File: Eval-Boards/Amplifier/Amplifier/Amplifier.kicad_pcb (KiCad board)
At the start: 2 copper layers, 1 part

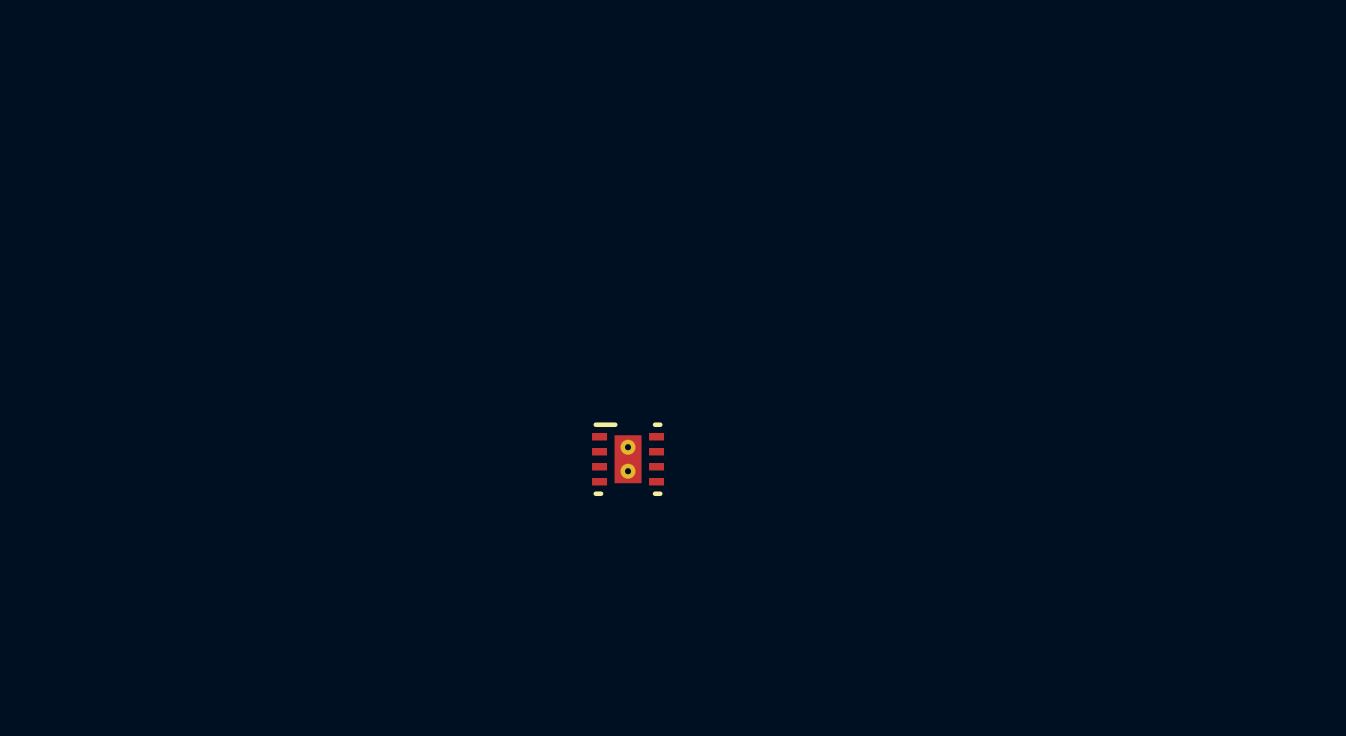
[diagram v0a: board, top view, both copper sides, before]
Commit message: New amplifier board
It looks really bad
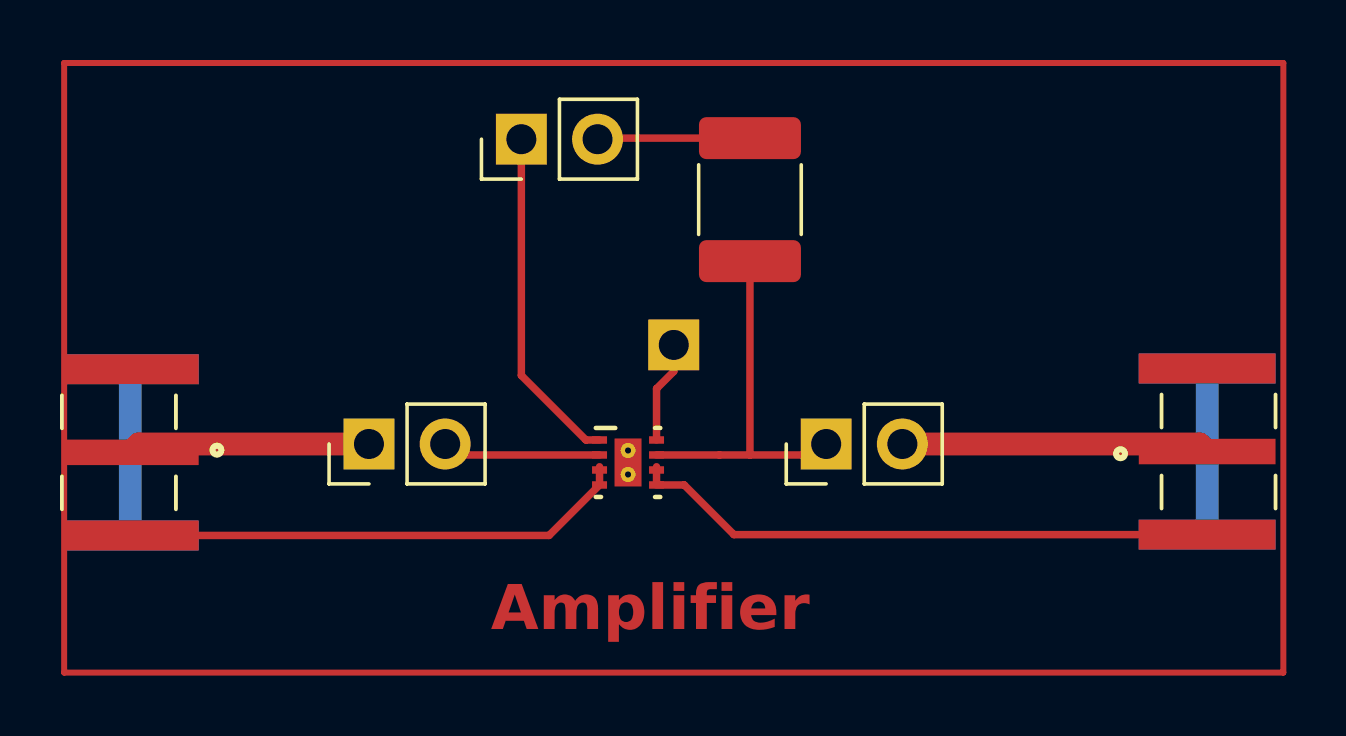
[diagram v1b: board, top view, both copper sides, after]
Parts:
- added ?: , , F.Cu at (61.0, 45.0)
- added REF**: TAOGLAS_EMPCB.SMAFSTJ.B.HT, SMA connectors:TAOGLAS_EMPCB.SMAFSTJ.B.HT, F.Cu at (42.8, 48.5)
- added REF**: PinHeader_1x02_P2.54mm_Vertical, Connector_PinHeader_2.54mm:PinHeader_1x02_P2.54mm_Vertical, F.Cu at (50.8, 48.3)
- added REF**: C_1812_4532Metric, Capacitor_SMD:C_1812_4532Metric, F.Cu at (63.5, 40.1)
- added REF**: PinHeader_1x02_P2.54mm_Vertical, Connector_PinHeader_2.54mm:PinHeader_1x02_P2.54mm_Vertical, F.Cu at (55.9, 38.1)
- added REF**: TAOGLAS_EMPCB.SMAFSTJ.B.HT, SMA connectors:TAOGLAS_EMPCB.SMAFSTJ.B.HT, F.Cu at (78.7, 48.5)
- added REF**: PinHeader_1x02_P2.54mm_Vertical, Connector_PinHeader_2.54mm:PinHeader_1x02_P2.54mm_Vertical, F.Cu at (66.0, 48.3)
- moved REF** 0.11 mm to (59.4, 48.9)
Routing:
- net (no net): track 0.00 -> 103.5 mm
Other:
- board text added: "Amplifier"

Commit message: Alot of stuff. Eval board for amp and VCO test
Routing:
- net (no net): track 103.5 -> 179.9 mm
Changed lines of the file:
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@@
   (gr_rect (start 40.64 35.56) (end 81.28 55.88)
     (stroke (width 0.2) (type default)) (fill none) (layer "F.Cu"))
-  (gr_text "Amplifier" (at 54.864 54.61) (layer "F.Cu")
+  (gr_text "Amplifier" (at 41.91 38.608) (layer "F.Cu")
     (effects (font (size 1.5 1.5) (thickness 0.3) bold) (justify left bottom))
   )
   (segment (start 63.5 48.625999) (end 65.674001 48.625999) (width 0.25) (layer "F.Cu") (net 0))
   (segment (start 53.705999 48.625999) (end 53.34 48.26) (width 0.25) (layer "F.Cu") (net 0))
+  (segment (start 75.184 53.594) (end 57.404 53.594) (width 2) (layer "F.Cu") (net 0))
   (segment (start 43.123001 48.26) (end 42.845001 48.538) (width 0.762) (layer "F.Cu") (net 0))
+  (segment (start 60.810001 49.126001) (end 61.309999 49.625999) (width 0.25) (layer "F.Cu") (net 0))
+  (segment (start 57.311998 50.8) (end 57.992999 50.118999) (width 0.25) (layer "F.Cu") (net 0))
+  (segment (start 61.214 49.625999) (end 61.309999 49.625999) (width 0.25) (layer "F.Cu") (net 0))
+  (segment (start 54.61 41.656) (end 56.896 43.942) (width 2) (layer "F.Cu") (net 0))
+  (segment (start 60.386001 49.625999) (end 61.214 49.625999) (width 0.25) (layer "F.Cu") (net 0))
+  (segment (start 61.214 53.594) (end 61.468 53.594) (width 0.25) (layer "F.Cu") (net 0))
+  (segment (start 58.485999 48.126) (end 58.032 48.126) (width 0.25) (layer "F.Cu") (net 0))
   (segment (start 50.8 48.26) (end 43.123001 48.26) (width 0.762) (layer "F.Cu") (net 0))
-  (segment (start 60.386001 49.625999) (end 61.309999 49.625999) (width 0.25) (layer "F.Cu") (net 0))
+  (segment (start 60.386001 49.126001) (end 60.810001 49.126001) (width 0.25) (layer "F.Cu") (net 0))
+  (segment (start 57.404 44.45) (end 57.404 44.958) (width 2) (layer "F.Cu") (net 0))
+  (segment (start 58.42 45.974) (end 58.166 45.72) (width 0.25) (layer "F.Cu") (net 0))
+  (segment (start 58.485999 49.126001) (end 58.061999 49.126001) (width 0.25) (layer "F.Cu") (net 0))
+  (segment (start 58.039 44.45) (end 57.404 44.45) (width 2) (layer "F.Cu") (net 0))
   (segment (start 60.386001 48.625999) (end 62.484 48.625999) (width 0.25) (layer "F.Cu") (net 0))
+  (segment (start 58.928 46.482) (end 58.928 45.212) (width 0.25) (layer "F.Cu") (net 0))
+  (segment (start 58.032 48.126) (end 52.07 42.164) (width 0.25) (layer "F.Cu") (net 0))
+  (segment (start 57.404 53.594) (end 58.928 52.07) (width 2) (layer "F.Cu") (net 0))
   (segment (start 60.386001 46.416001) (end 60.96 45.842002) (width 0.25) (layer "F.Cu") (net 0))
   (segment (start 65.674001 48.625999) (end 66.04 48.26) (width 0.25) (layer "F.Cu") (net 0))
@@
   (segment (start 78.625251 48.625999) (end 78.74 48.51125) (width 0.25) (layer "F.Cu") (net 0))
   (segment (start 56.803998 51.308) (end 42.845001 51.308) (width 0.25) (layer "F.Cu") (net 0))
+  (segment (start 57.404 53.594) (end 45.974 53.594) (width 2) (layer "F.Cu") (net 0))
   (segment (start 68.58 48.26) (end 78.48875 48.26) (width 0.762) (layer "F.Cu") (net 0))
+  (segment (start 56.896 43.942) (end 57.404 44.45) (width 2) (layer "F.Cu") (net 0))
+  (segment (start 56.642 42.164) (end 58.039 42.164) (width 2) (layer "F.Cu") (net 0))
+  (segment (start 52.07 41.148) (end 55.118 38.1) (width 0.25) (layer "F.Cu") (net 0))
+  (segment (start 52.07 42.164) (end 52.07 41.148) (width 0.25) (layer "F.Cu") (net 0))
+  (segment (start 58.061999 49.126001) (end 56.642 50.546) (width 0.25) (layer "F.Cu") (net 0))
+  (segment (start 58.928 46.482) (end 58.674 46.228) (width 0.25) (layer "F.Cu") (net 0))
+  (segment (start 58.928 52.07) (end 61.214 52.07) (width 2) (layer "F.Cu") (net 0))
   (segment (start 60.386001 48.126) (end 60.386001 46.416001) (width 0.25) (layer "F.Cu") (net 0))
-  (segment (start 56.803998 51.308) (end 58.485999 49.625999) (width 0.25) (layer "F.Cu") (net 0))
+  (segment (start 59.69 41.148) (end 55.118 41.148) (width 2) (layer "F.Cu") (net 0))
   (segment (start 60.96 45.842002) (end 60.96 44.958) (width 0.25) (layer "F.Cu") (net 0))
-  (segment (start 60.386001 49.517998) (end 60.386001 49.018) (width 0.25) (layer "F.Cu") (net 0))
-  (segment (start 58.485999 48.126) (end 58.032 48.126) (width 0.25) (layer "F.Cu") (net 0))
+  (segment (start 59.436 49.276) (end 59.436 50.8) (width 0.5) (layer "F.Cu") (net 0))
+  (segment (start 56.803998 51.308) (end 57.992999 50.118999) (width 0.25) (layer "F.Cu") (net 0))
+  (segment (start 58.674 46.228) (end 58.42 45.974) (width 0.25) (layer "F.Cu") (net 0))
+  (segment (start 60.071 41.529) (end 59.69 41.148) (width 2) (layer "F.Cu") (net 0))
   (segment (start 62.484 48.625999) (end 63.5 48.625999) (width 0.25) (layer "F.Cu") (net 0))
+  (segment (start 56.896 43.307) (end 56.896 43.942) (width 2) (layer "F.Cu") (net 0))
+  (segment (start 59.436 48.476002) (end 59.436 46.99) (width 0.5) (layer "F.Cu") (net 0))
+  (segment (start 61.214 52.07) (end 62.738 53.594) (width 2) (layer "F.Cu") (net 0))
   (segment (start 61.309999 49.625999) (end 62.96525 51.28125) (width 0.25) (layer "F.Cu") (net 0))
-  (segment (start 58.485999 49.018) (end 58.485999 49.517998) (width 0.25) (layer "F.Cu") (net 0))
+  (segment (start 59.436 51.816) (end 59.69 52.07) (width 0.25) (layer "F.Cu") (net 0))
+  (segment (start 58.039 42.164) (end 59.182 43.307) (width 2) (layer "F.Cu") (net 0))
   (segment (start 63.5 38.064) (end 58.456 38.064) (width 0.25) (layer "F.Cu") (net 0))
-  (segment (start 55.88 45.974) (end 55.88 38.1) (width 0.25) (layer "F.Cu") (net 0))
   (segment (start 42.933 48.625999) (end 42.845001 48.538) (width 0.25) (layer "F.Cu") (net 0))
+  (segment (start 56.642 50.546) (end 56.642 51.308) (width 0.25) (layer "F.Cu") (net 0))
+  (segment (start 59.436 46.99) (end 58.928 46.482) (width 0.5) (layer "F.Cu") (net 0))
+  (segment (start 60.071 42.418) (end 59.182 43.307) (width 2) (layer "F.Cu") (net 0))
+  (segment (start 57.992999 50.118999) (end 58.485999 49.625999) (width 0.25) (layer "F.Cu") (net 0))
+  (segment (start 60.071 42.418) (end 60.071 41.529) (width 2) (layer "F.Cu") (net 0))
+  (segment (start 59.182 43.307) (end 58.039 44.45) (width 2) (layer "F.Cu") (net 0))
   (segment (start 63.5 48.625999) (end 63.5 42.164) (width 0.25) (layer "F.Cu") (net 0))
+  (segment (start 59.436 50.8) (end 59.436 51.816) (width 0.5) (layer "F.Cu") (net 0))
+  (segment (start 58.039 42.164) (end 56.896 43.307) (width 2) (layer "F.Cu") (net 0))
+  (segment (start 62.738 53.594) (end 61.468 53.594) (width 2) (layer "F.Cu") (net 0))
   (segment (start 58.456 38.064) (end 58.42 38.1) (width 0.25) (layer "F.Cu") (net 0))
-  (segment (start 58.032 48.126) (end 55.88 45.974) (width 0.25) (layer "F.Cu") (net 0))
+  (segment (start 55.118 38.1) (end 55.88 38.1) (width 0.25) (layer "F.Cu") (net 0))
+  (segment (start 57.404 44.958) (end 58.42 45.974) (width 2) (layer "F.Cu") (net 0))
   (segment (start 58.485999 48.625999) (end 53.705999 48.625999) (width 0.25) (layer "F.Cu") (net 0))
   (segment (start 78.48875 48.26) (end 78.74 48.51125) (width 0.762) (layer "F.Cu") (net 0))
+  (segment (start 59.436 50.8) (end 59.436 53.848) (width 0.4) (layer "F.Cu") (net 0))
   (segment (start 78.74 45.74125) (end 78.74 51.28125) (width 0.762) (layer "B.Cu") (net 0))
   (segment (start 42.845001 45.768) (end 42.845001 51.308) (width 0.762) (layer "B.Cu") (net 0))
